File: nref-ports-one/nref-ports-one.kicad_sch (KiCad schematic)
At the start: 150 parts, among them J1 CONN_HEAD, J10 CONN_SPK, J11 POWSW, J2 DM3AT-SF-PEJM5, J3 09452812561, J4 USB_C_Receptacle, J5 Conn_01x10_Pin, J6 Conn_01x14_Pin, J7 Conn_01x12_Pin, J8 PWR, J9 Conn_01x10_Pin, SW1 SW_Push, U1 TPS7A0533PDBZ, U10 LMR51430, U11 TPS66021YBGR, U12 TLV75518PDBV, U13 TMUXHS4212, U14 EQCO5X31C0-I_6NX, U15 LP5907MFX-1.2, U2 TLV320AIC3100, U3 TXS0108EPW, U4 SN74AVC1T45, U5 TPD4E02B04DQA, U6 TPD4E02B04DQA, U7 TPD4E02B04DQA, U8 FUSB302BMPX, U9 PCA9557BS

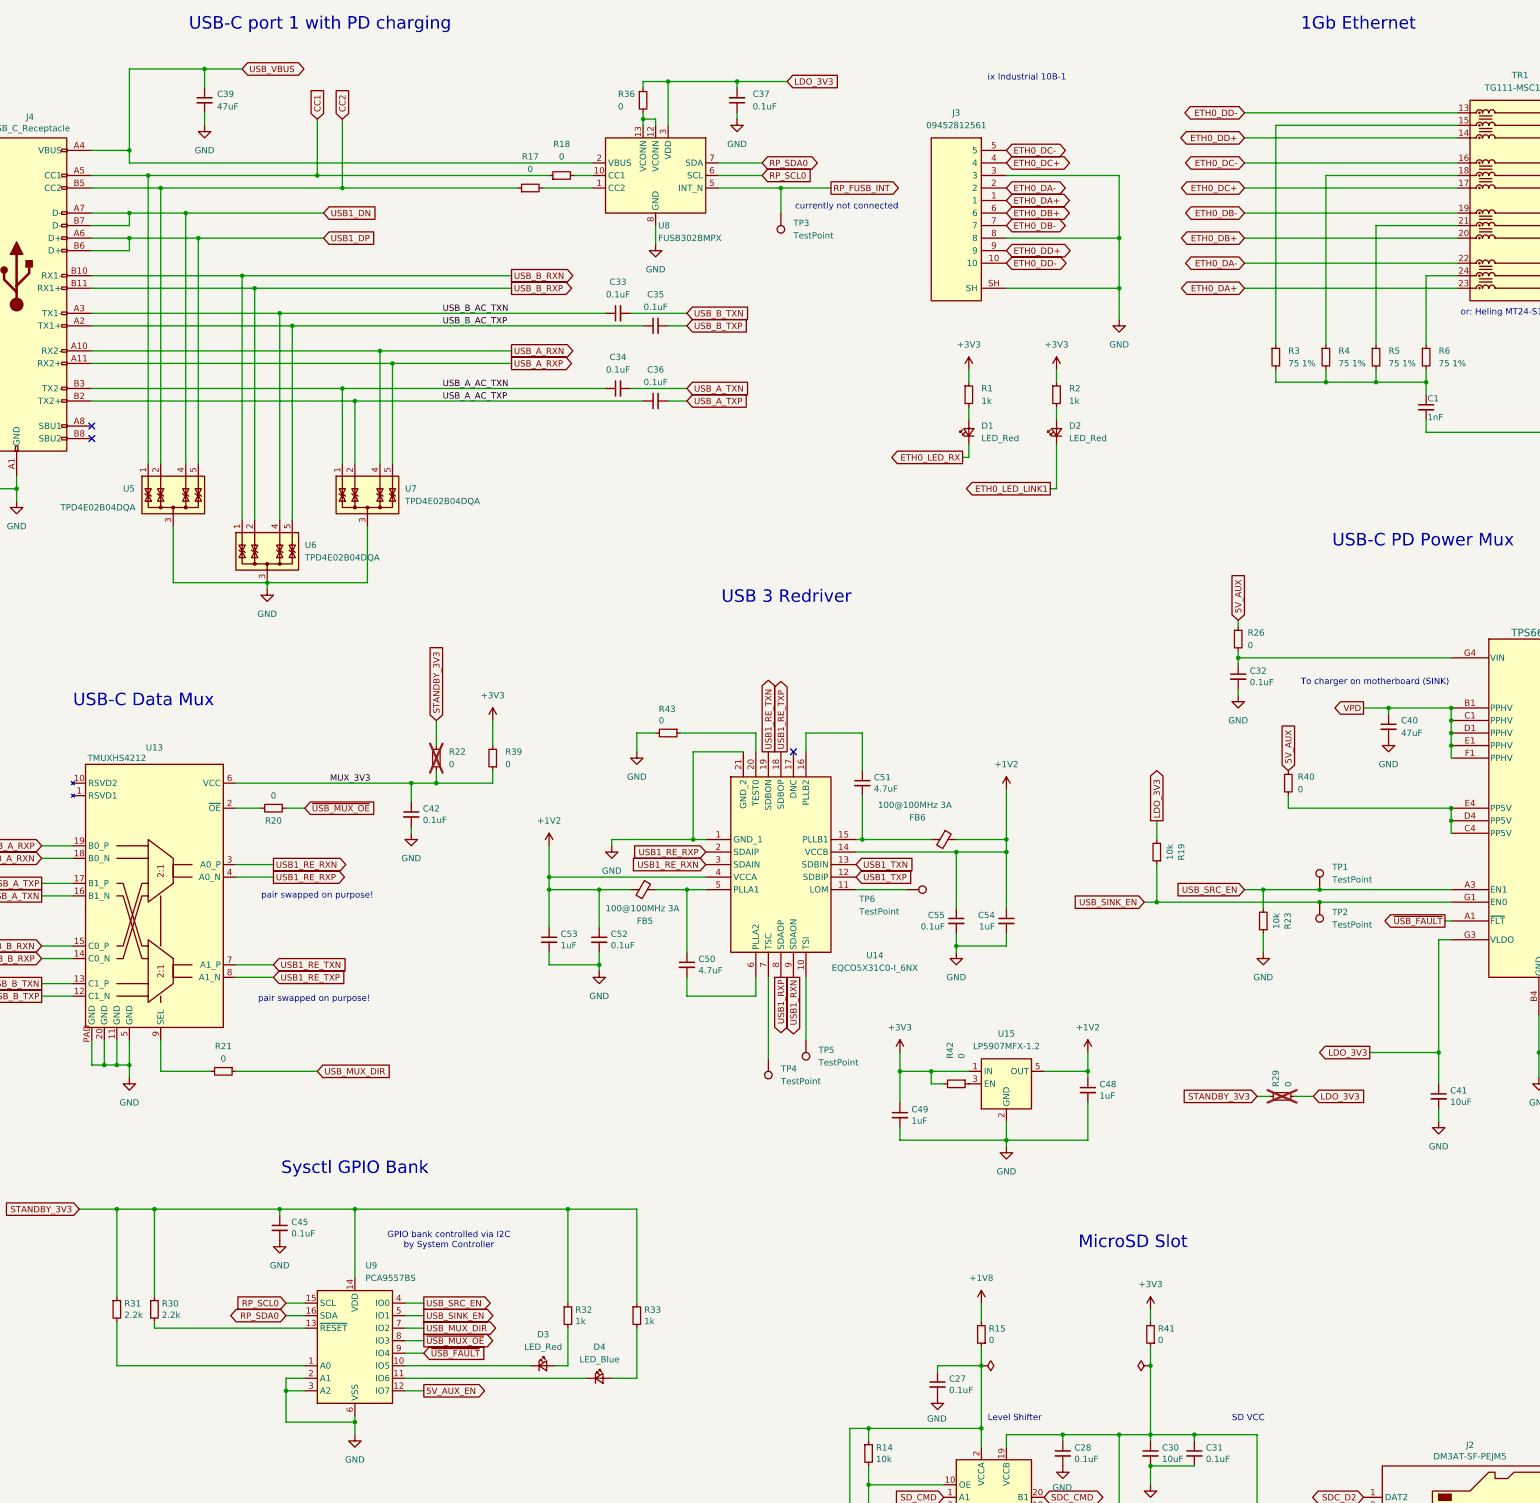
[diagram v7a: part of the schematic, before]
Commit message: ports-one: exchange pca chip, polish, add sbu header
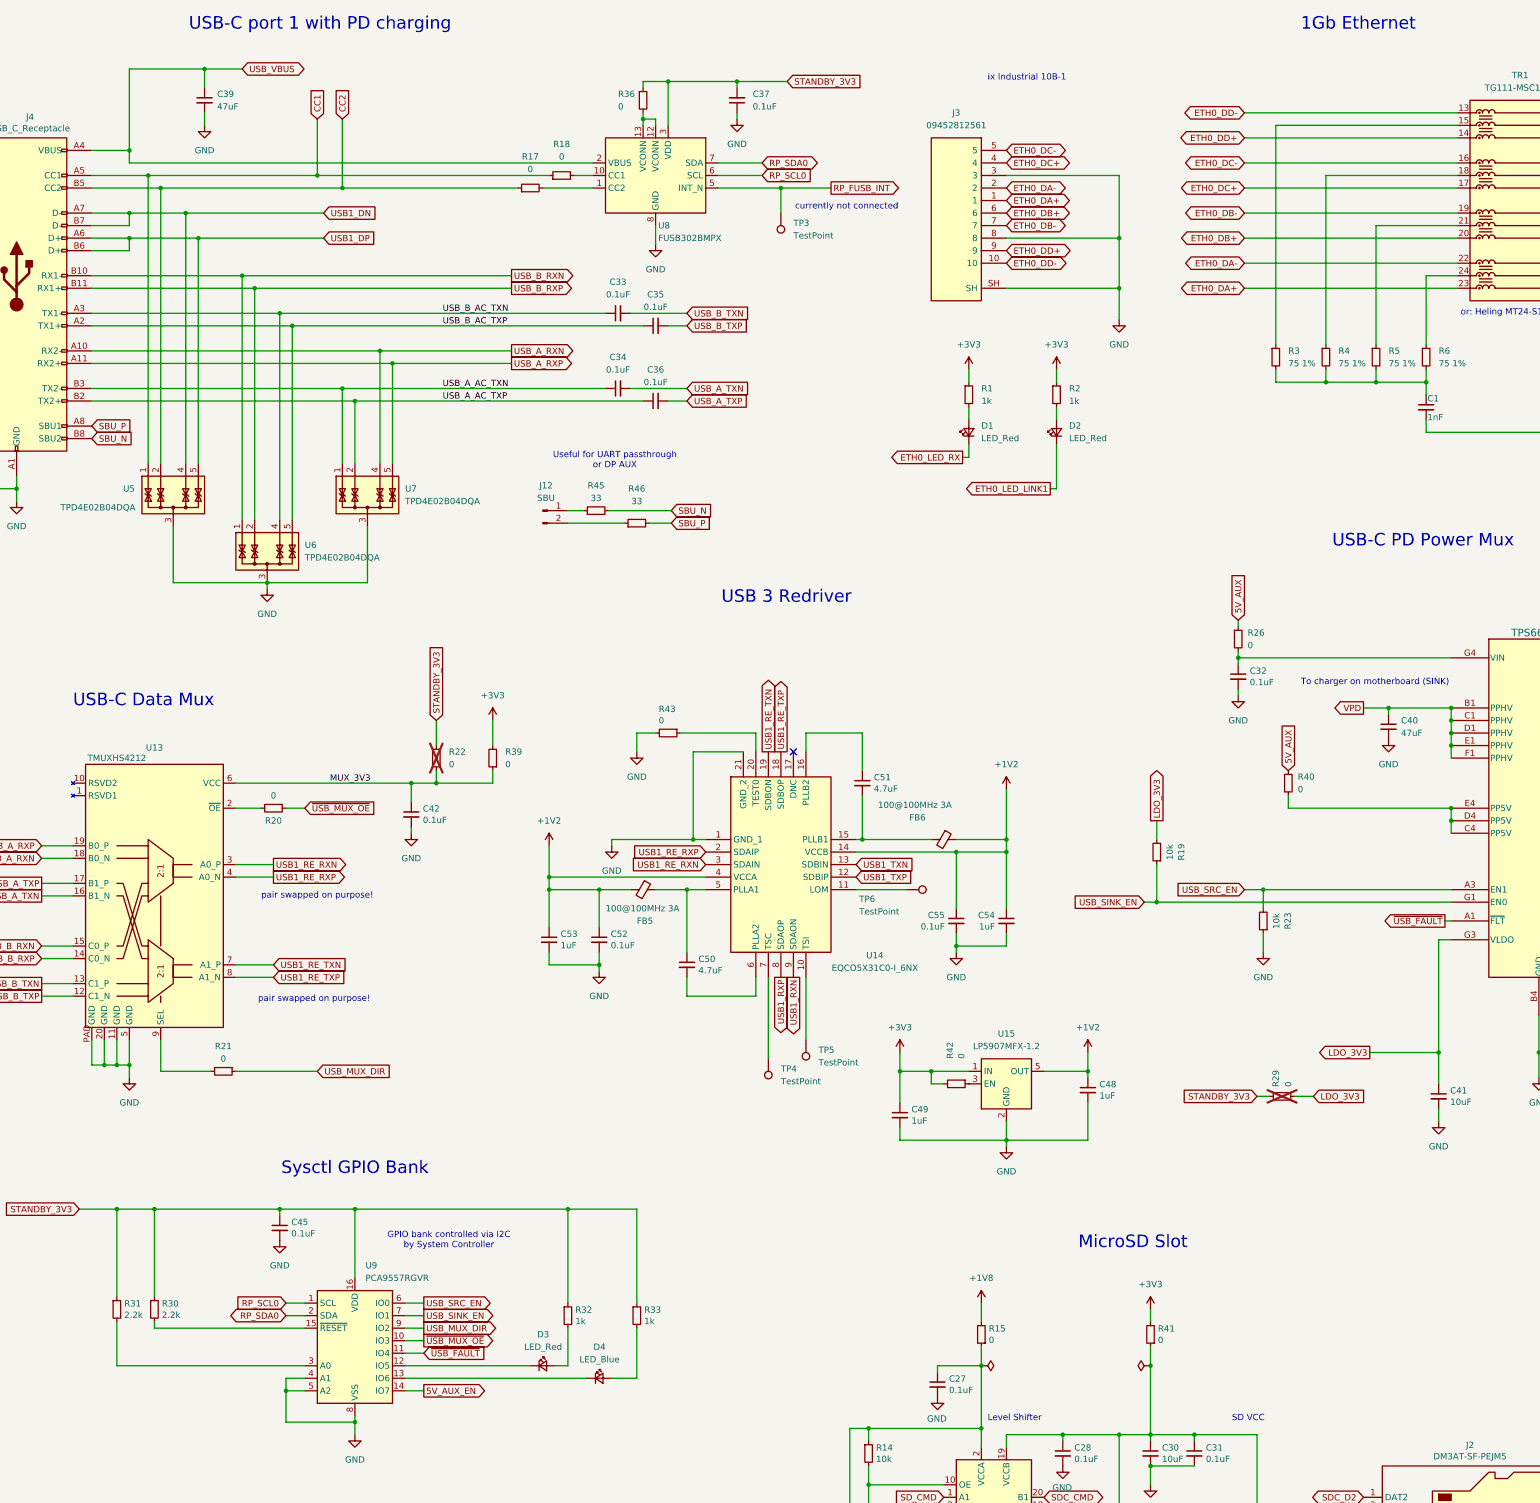
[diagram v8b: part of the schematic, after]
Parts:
- removed TP1, TP2: TestPoint, TestPoint:TestPoint_Pad_D1.0mm, symbol Connector:TestPoint
- removed U9: PCA9557BS, Package_DFN_QFN:HVQFN-16-1EP_3x3mm_P0.5mm_EP1.5x1.5mm, symbol Interface_Expansion:PCA9557BS
- added J12: SBU, Connector_JST:JST_SH_SM02B-SRSS-TB_1x02-1MP_P1.00mm_Horizontal, symbol Connector:Conn_01x02_Pin
- added R45, R46: 33, Resistor_SMD:R_0402_1005Metric, symbol Device:R_Small
- added U9: PCA9557RGVR, Package_DFN_QFN:Texas_RSA_VQFN-16-1EP_4x4mm_P0.65mm_EP2.7x2.7mm, symbol Interface_Expansion:PCA9557PW
- C41, C47: Manufacturer Yageo -> Samsung; Manufacturer_No CC0402KRX5R6BB105 -> CL10A106MO8NQNC
- C43, C44, C48, C49, C53, C54: Manufacturer Yageo -> Samsung; Manufacturer_No CC0402KRX5R6BB105 -> CL05B104KO5NNNC
- D1, D2, D3, D4: Manufacturer_No 19-217/R6C-AL1M2VY/3T -> (none)
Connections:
- net 5V_AUX_EN: now also U9.14 (IO7)
- net GND: now also U9.4 (A1), U9.5 (A2), U9.8 (VSS)
- net LDO_3V3: no longer C37.2, R36.1, U8.3 (VDD), U8.4 (VDD)
- net RP_SCL0: now also U9.1 (SCL)
- net RP_SDA0: now also U9.2 (SDA)
- net STANDBY_3V3: now also C37.2, R36.1, U8.3 (VDD), U8.4 (VDD), U9.16 (VDD)
- net USB_MUX_DIR: now also U9.9 (IO2)
- net USB_SINK_EN: now also U9.7 (IO1)
- net USB_SRC_EN: now also U9.6 (IO0)
- net ~{USB_FAULT}: now also U9.11 (IO4)
- net ~{USB_MUX_OE}: now also U9.10 (IO3)
- net at D3.1 (K): now also U9.12 (IO5)
- net at R30.2: now also U9.15 (~{RESET})
- net at D4.1 (K): now also U9.13 (IO6)
- net at R31.2: now also U9.3 (A0)
- net SBU_P: now reaches J4.A8 (SBU1)
- net SBU_P: now also R46.2
- net SBU_N: now reaches J4.B8 (SBU2)
- net SBU_N: now also R45.2
- new net: J12.2 (Pin_2), R46.1
- new net: J12.1 (Pin_1), R45.1
- no-connect marks 12 -> 10
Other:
- note added: "Useful for UART passthrough or DP AUX"
